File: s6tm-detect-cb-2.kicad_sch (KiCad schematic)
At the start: 0 parts

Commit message: schem: add esp32-s3
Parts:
- added AE1: Antenna, RF_Antenna:Johanson_2450AT18x100, symbol Device:Antenna
- added C10, C11, C12, C8: 0u1, Capacitor_SMD:C_0402_1005Metric, symbol Device:C
- added C13, C6, C9: 1u, Capacitor_SMD:C_0402_1005Metric, symbol Device:C
- added C3, C5: 1p2, Capacitor_SMD:C_0402_1005Metric, symbol Device:C
- added C7: 10u, Capacitor_SMD:C_0402_1005Metric, symbol Device:C
- added J5: Conn_01x04_Pin, Connector_PinHeader_2.54mm:PinHeader_1x04_P2.54mm_Vertical, symbol Connector:Conn_01x04_Pin
- added L1: 6n8, Inductor_SMD:L_0402_1005Metric, symbol Device:L
- added L2: L, Inductor_SMD:L_0402_1005Metric, symbol Device:L
- added L3, L4: 2n7, Inductor_SMD:L_0402_1005Metric, symbol Device:L
- added R20: 470, Resistor_SMD:R_0402_1005Metric, symbol Device:R
- added R21, R22: 22, Resistor_SMD:R_0402_1005Metric, symbol Device:R
- added R23, R7: 10k, Resistor_SMD:R_0402_1005Metric, symbol Device:R
- added R6: 0, Resistor_SMD:R_0402_1005Metric, symbol Device:R
- added U3: ESP32-S3FN8, Package_DFN_QFN:QFN-56-1EP_7x7mm_P0.4mm_EP5.6x5.6mm, symbol PCM_Espressif:ESP32-S3
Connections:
- new net: J5.4 (Pin_4), R20.1
- new net: L1.2, L2.1, R6.1
- new net +3V3: C11.1, C12.1, C13.1, C7.1, C8.1, J5.1 (Pin_1), L4.1, R23.2, R7.1, U3.20 (VDD3P3_RTC), U3.46 (VDD3P3_CPU), U3.55 (VDDA), U3.56 (VDDA)
- new net BOOT: R23.1, U3.5 (GPIO0/BOOT)
- new net CHIP_PU: C6.1, R7.2, U3.4 (CHIP_PU/RESET)
- new net D+: R21.2
- new net D-: R22.2
- new net ESP_D+: R21.1, U3.26 (GPIO20/USB_D+/ADC2_CH9)
- new net ESP_D-: R22.1, U3.25 (GPIO19/USB_D-/ADC2_CH8)
- new net GND: C10.2, C11.2, C12.2, C13.2, C3.2, C5.2, C6.2, C7.2, C8.2, C9.2, J5.3 (Pin_3), U3.57 (GND)
- new net RF_ANT: AE1.1 (A), L1.1
- new net RF_ESP: C5.1, L3.2
- new net RF_TRANS: C3.1, L3.1, R6.2
- new net U0RXD: J5.2 (Pin_2), U3.50 (U0RXD/PROG/GPIO44)
- new net U0TXD: R20.2, U3.49 (U0TXD/PROG/GPIO43)
- new net VDD3P3: C10.1, L4.2, U3.2 (VDD3P3), U3.3 (VDD3P3)
- new net VDD_SPI: C9.1, U3.29 (VDD_SPI)
- new net XTAL_N: U3.53 (XTAL_N)
- new net XTAL_P: U3.54 (XTAL_P)
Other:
- note added: "EN RC delay"
- note added: "UART"

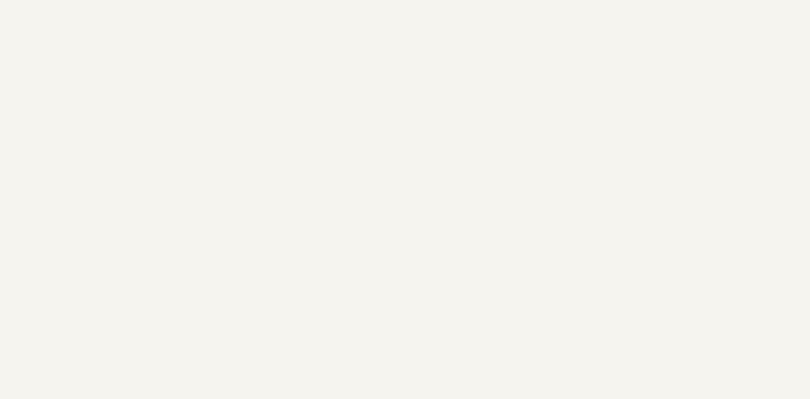
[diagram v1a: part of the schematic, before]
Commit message: schem: add hse crystal
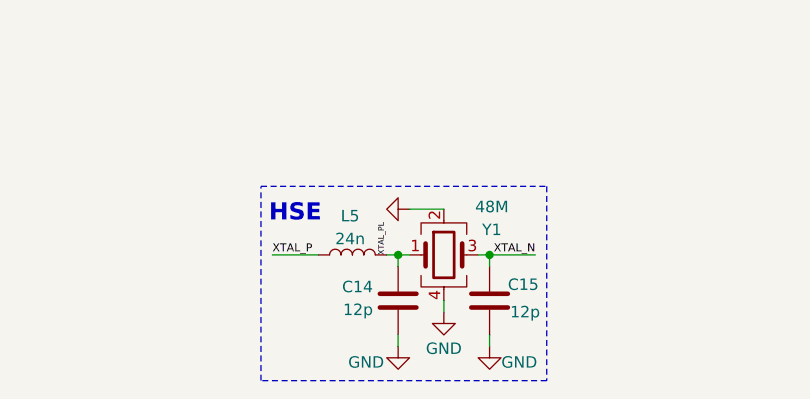
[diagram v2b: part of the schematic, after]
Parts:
- added C14, C15: 12p, Capacitor_SMD:C_0402_1005Metric, symbol Device:C
- added L5: 24n, Inductor_SMD:L_0402_1005Metric, symbol Device:L
- added Y1: 48M, Crystal:Crystal_SMD_2016-4Pin_2.0x1.6mm, symbol Device:Crystal_GND24
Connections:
- net GND: now also C14.1, C15.2, Y1.2, Y1.4
- net XTAL_N: now also C15.1, Y1.3
- net XTAL_P: now also L5.1
- new net XTAL_PL: C14.2, L5.2, Y1.1
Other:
- note added: "HSE"

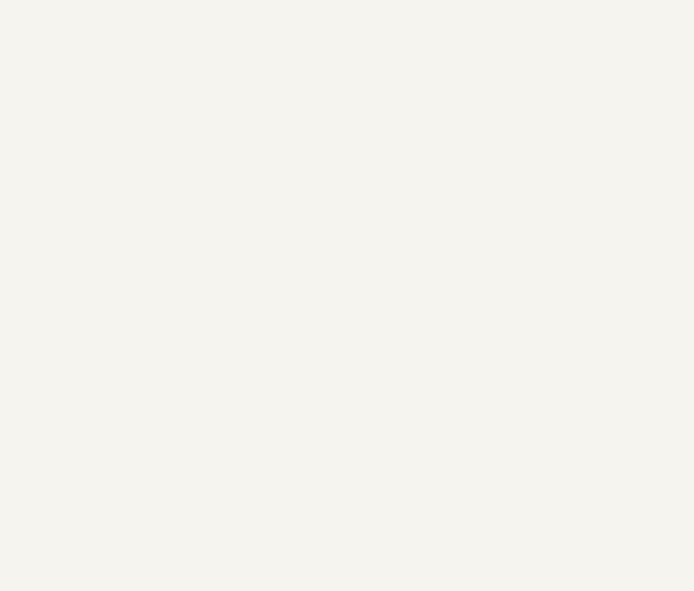
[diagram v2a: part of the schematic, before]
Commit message: schem: add usb-c connector
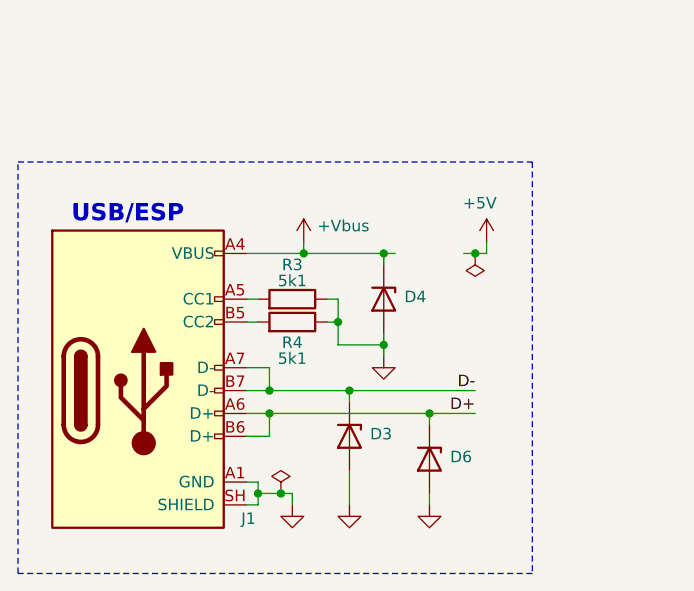
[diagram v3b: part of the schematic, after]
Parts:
- added D3, D4, D6: H5VU10U, GLCS:Diode_DFN1006, symbol GLCS:H5VU10U
- added J1: USB_C_Receptacle_USB2.0_14P, Connector_USB:USB_C_Receptacle_HRO_TYPE-C-31-M-12, symbol Connector:USB_C_Receptacle_USB2.0_14P
- added R3, R4: 5k1, Resistor_SMD:R_0402_1005Metric, symbol Device:R
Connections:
- net D+: now also D6.1 (K), J1.A6 (D+), J1.B6 (D+)
- net D-: now also D3.1 (K), J1.A7 (D-), J1.B7 (D-)
- net GND: now also D3.2 (A), D4.2 (A), D6.2 (A), J1.A1 (GND), J1.A12 (GND), J1.B1 (GND), J1.B12 (GND), J1.SH (SHIELD), R3.1, R4.1
- new net: J1.A5 (CC1), R3.2
- new net: J1.B5 (CC2), R4.2
- new net +Vbus: D4.1 (K), J1.A4 (VBUS), J1.A9 (VBUS), J1.B4 (VBUS), J1.B9 (VBUS)
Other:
- note added: "USB/ESP"

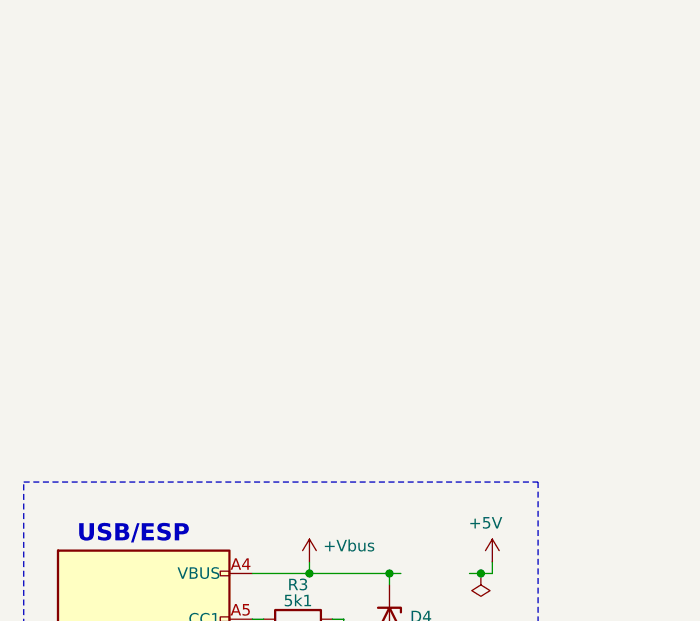
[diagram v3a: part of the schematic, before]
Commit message: schem: add can transceiver
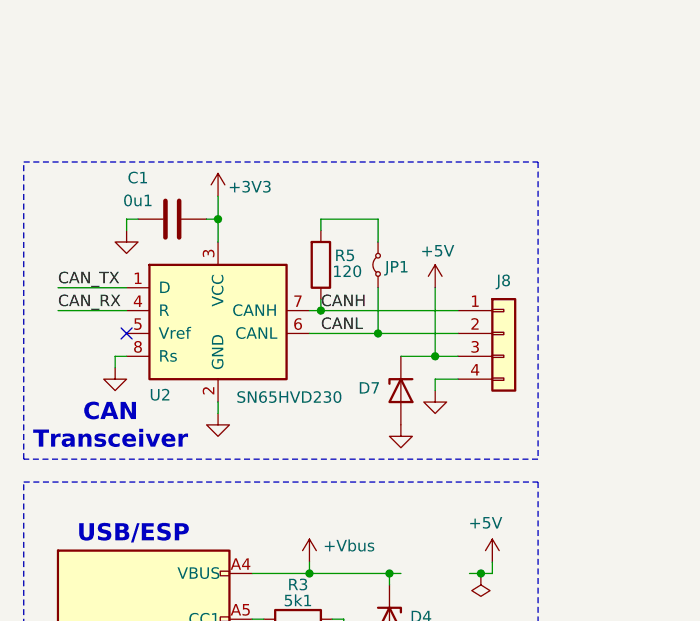
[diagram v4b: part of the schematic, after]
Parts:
- added C1: 0u1, Capacitor_SMD:C_0402_1005Metric, symbol Device:C
- added D7: H5VU10U, GLCS:Diode_DFN1006, symbol GLCS:H5VU10U
- added J8: Conn_01x04, Connector_JST:JST_XH_S4B-XH-A-1_1x04_P2.50mm_Horizontal, symbol Connector_Generic:Conn_01x04
- added JP1: Jumper_2_Small_Bridged, Jumper:SolderJumper-2_P1.3mm_Open_RoundedPad1.0x1.5mm, symbol Jumper:Jumper_2_Small_Bridged
- added R5: 120, Resistor_SMD:R_1206_3216Metric, symbol Device:R
- added U2: SN65HVD230, Package_SO:SOIC-8_3.9x4.9mm_P1.27mm, symbol Interface_CAN_LIN:SN65HVD230
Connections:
- net +3V3: now also C1.1, U2.3 (VCC)
- net +5V: now also D7.1 (K), J8.3 (Pin_3)
- net GND: now also C1.2, D7.2 (A), J8.4 (Pin_4), U2.2 (GND), U2.8 (Rs)
- new net: JP1.2 (B), R5.2
- new net CANH: J8.1 (Pin_1), R5.1, U2.7 (CANH)
- new net CANL: J8.2 (Pin_2), JP1.1 (A), U2.6 (CANL)
- new net CAN_RX: U2.4 (R)
- new net CAN_TX: U2.1 (D)
- no-connect marks 0 -> 1
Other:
- note added: "CAN Transceiver"

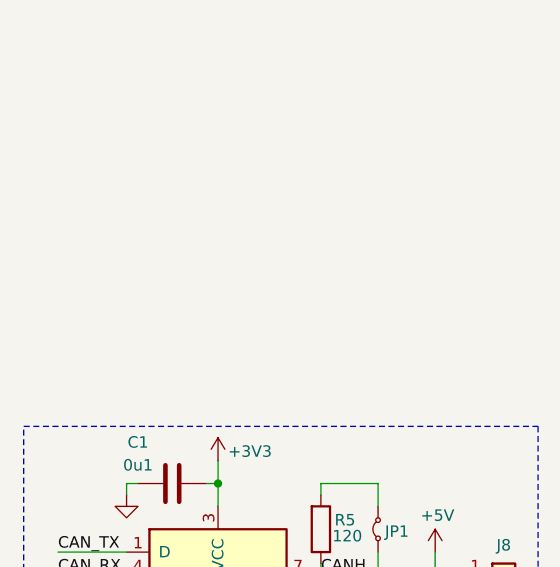
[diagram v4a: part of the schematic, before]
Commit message: schem: add buttons
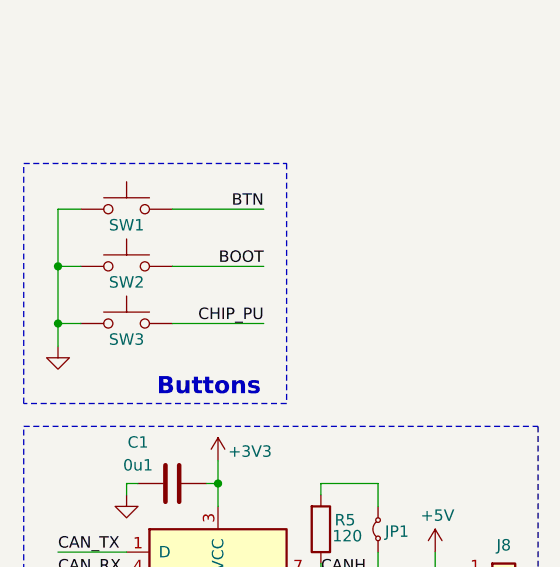
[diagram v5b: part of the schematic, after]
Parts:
- added SW1, SW2, SW3: SW_Push, Button_Switch_SMD:SW_SPST_TS-1088-xR020, symbol Switch:SW_Push
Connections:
- net BOOT: now also SW2.2
- net CHIP_PU: now also SW3.2
- net GND: now also SW1.1, SW2.1, SW3.1
- new net BTN: SW1.2
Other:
- note added: "Buttons"

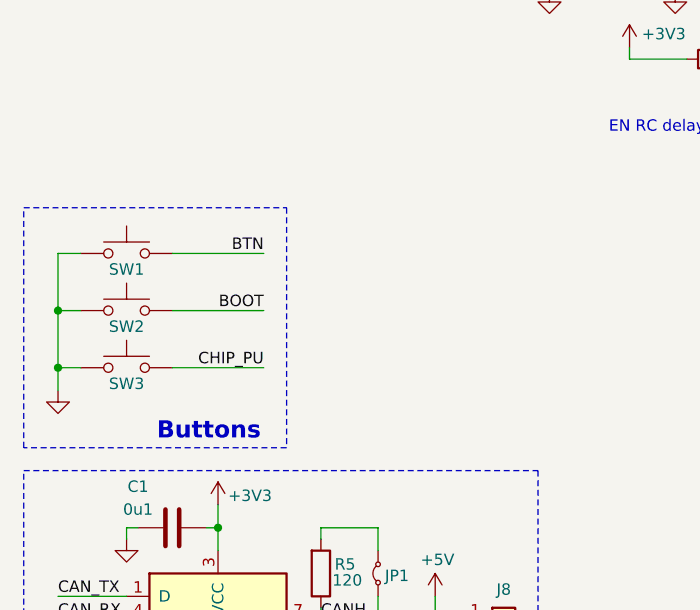
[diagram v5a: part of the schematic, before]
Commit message: schem: add WS2812B RGB LED
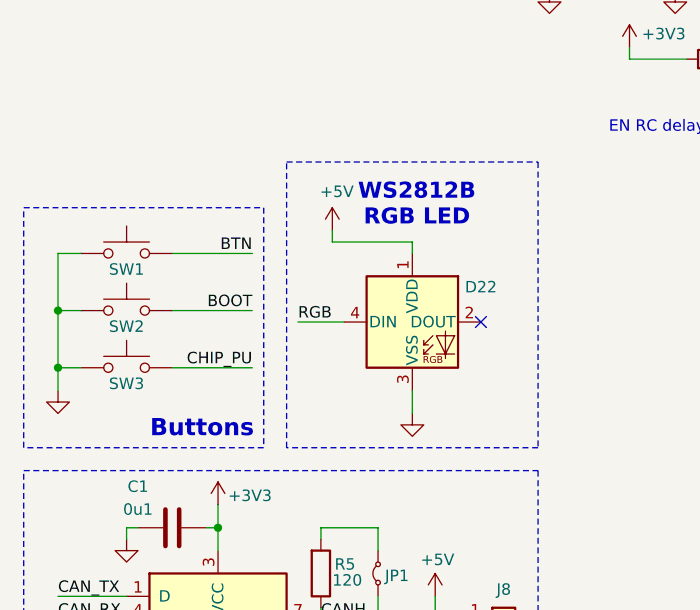
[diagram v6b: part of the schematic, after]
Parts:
- added D22: WS2812B, LED_SMD:LED_WS2812B_PLCC4_5.0x5.0mm_P3.2mm, symbol LED:WS2812B
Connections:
- net +5V: now also D22.1 (VDD)
- net GND: now also D22.3 (VSS)
- new net RGB: D22.4 (DIN)
- no-connect marks 1 -> 2
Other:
- note added: "WS2812B RGB LED"

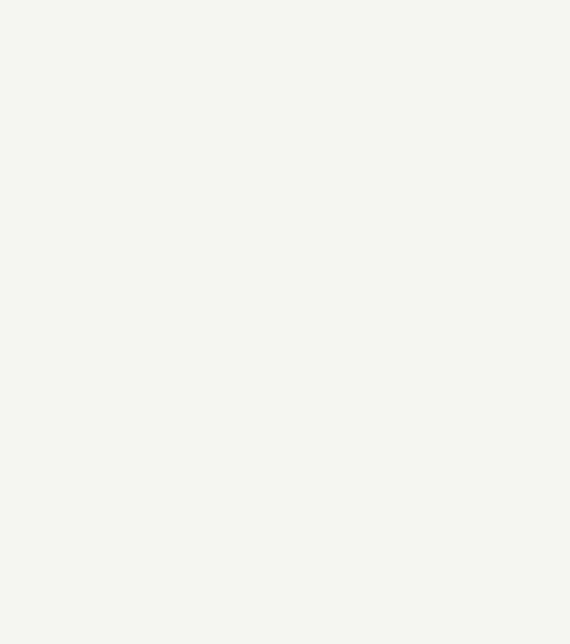
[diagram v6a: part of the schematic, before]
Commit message: schem: add nextpm 6pin connector
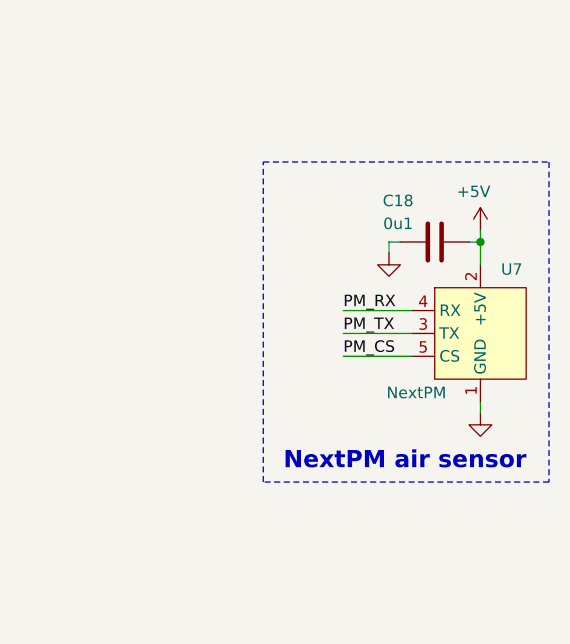
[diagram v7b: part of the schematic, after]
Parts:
- added C18: 0u1, Capacitor_SMD:C_0402_1005Metric, symbol Device:C
- added U7: NextPM, Connector_JST:JST_PH_S6B-PH-K_1x06_P2.00mm_Horizontal, symbol GLCS:NextPM
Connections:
- net +5V: now also C18.2, U7.2 (+5V)
- net GND: now also C18.1, U7.1 (GND), U7.6 (GND)
- new net PM_CS: U7.5 (CS)
- new net PM_RX: U7.4 (RX)
- new net PM_TX: U7.3 (TX)
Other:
- note added: "NextPM air sensor"

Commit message: schem: add smt assembly fids and tooling holes
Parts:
- added FID1, FID2, FID3: Fiducial, Fiducial:Fiducial_1mm_Mask2mm, symbol Mechanical:Fiducial
- added H1, H2, H3: MountingHole, MountingHole:ToolingHole_1.152mm, symbol Mechanical:MountingHole
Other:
- note added: "SMT assembly"
